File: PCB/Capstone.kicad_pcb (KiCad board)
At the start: 2 copper layers, 241 parts, among them J1 S2B-PH-SM4-TB, J10 DNP, J11 DNP, J12 PH1-08-UA, J13 DNP, J14 DNP, J15 DNP, J2 TRANSDUCER, J3 DNP, J4 PH1-08-UA, J5 DNP, J6 DNP, J7 DNP, J8 DNP, J9 DNP, Q1 SSM6K361NU, SW1 SW_Push, SW2 SW_Push, SW3 SW_Push, U1 TPS63031, U10 AP2204K-ADJ, U11 LM3478, U12 10CL010, U13 ECS-5032MV, U14 TSX9291, U15 LTC6090-5, U16 AD5450, U17 ADA4522-1, U18 MAX5394L, U19 MAX5394L, U2 TCR2EF25, U20 MAX11116, U21 TLV3544, U22 MCP6L1, U3 TPS62262, U4 BMD-360, U5 MIC841N, U6 ENS210, U7 W25Q80DV, U8 LIS2DE12, U9 LMR62421

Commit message: Begin layout around FPGA and microcontroller, rearrange some connections to FPGA and microcontroller, change groupings of optional debug pins
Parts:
- removed the C57 at (126.5, 83.0)
- removed the J12 at (82.3, 100.6)
- removed J15: DNP, Pin_Headers:Pin_Header_Straight_1x03_Pitch2.54mm
- added C51: 2.2nF, Capacitors_SMD:C_0603_HandSoldering, F.Cu at (131.2, 150.9)
- added C58: 22nF, Capacitors_SMD:C_0603_HandSoldering, F.Cu at (118.7, 152.3)
- added J14: DNP, Pin_Headers:Pin_Header_Straight_1x04_Pitch2.54mm, F.Cu at (186.1, 83.8)
- C49: value 2.2nF -> 100nF
- J10: footprint Pin_Headers:Pin_Header_Straight_1x03_Pitch2.54mm -> Pin_Headers:Pin_Header_Straight_1x05_Pitch2.54mm
- J11: footprint Pin_Headers:Pin_Header_Straight_1x03_Pitch2.54mm -> Pin_Headers:Pin_Header_Straight_2x05_Pitch2.54mm
- moved R13 111.3 mm to (85.1, 152.9), turned to 180 degrees
- moved SW2 107.7 mm to (85.1, 158.8), turned to 270 degrees
- moved R12 93.8 mm to (76.2, 152.9), turned to 180 degrees
- moved SW1 92.3 mm to (76.2, 158.8), turned to 270 degrees
- moved C49 79.9 mm to (133.3, 162.3), turned to 270 degrees
- moved J4 74.5 mm to (47.5, 128.5), turned to 0 degrees
- moved R38 73.5 mm to (136.4, 157.3), turned to 90 degrees
- moved J11 73.2 mm to (130.8, 160.0), turned to 270 degrees
- moved C59 70.7 mm to (131.2, 152.3), turned to 0 degrees
- moved C50 68.0 mm to (118.7, 150.9), turned to 180 degrees
- moved C47 67.4 mm to (135.0, 150.9), turned to 0 degrees
- moved C72 66.8 mm to (125.0, 152.0), turned to 270 degrees
- moved R39 66.1 mm to (126.7, 157.4), turned to 0 degrees
- moved C45 65.7 mm to (137.9, 148.3), turned to 0 degrees
- moved C60 65.3 mm to (139.6, 142.5), turned to 90 degrees
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- renumbered C99 to C100, C100 to C101, C101 to C102, C102 to C103, C103 to C104, C51 to C52, C52 to C53, C53 to C54, C54 to C55, C55 to C56, C56 to C57, C58 to C59, C59 to C60, C60 to C61, C61 to C62, C62 to C63, C63 to C64, C64 to C65, C65 to C66, C66 to C67, C67 to C68, C68 to C69, C69 to C70, C70 to C71, C71 to C72, C72 to C73, C73 to C74, C74 to C75, C75 to C76, C76 to C77, C77 to C78, C78 to C79, C79 to C80, C80 to C81, C81 to C82, C82 to C83, C83 to C84, C84 to C85, C85 to C86, C86 to C87, C87 to C88, C88 to C89, C89 to C90, C90 to C91, C91 to C92, C92 to C93, C93 to C94, C94 to C95, C95 to C96, C96 to C97, C97 to C98, C98 to C99, J13 to J12, J14 to J13
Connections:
- C47 pad 2: GND -> GNDA-FPGA
- C48 pad 2: GND -> GNDA-FPGA
- C49 pad 1: +1V2 -> +2V5
- C49 pad 2: GND -> GNDA-FPGA
- J10 pad 1: VGA-SCK -> VGA-~CS0
- J10 pad 3: VGA-~CS0 -> VGA-SCK
- J11 pad 1: TRANSMIT-ENABLE -> FPGA-TCK
- J11 pad 2: VGA-~CS1 -> GND
- J11 pad 3: VGA-D1 -> FPGA-TDO
- U12 pad 1: FPGA-LINK0 -> (no net)
- U12 pad 10: Net-(U12-Pad10) -> (no net)
- U12 pad 100: DAC-~CS -> (no net)
- U12 pad 101: DAC-SDI -> Net-(U12-Pad101)
- U12 pad 103: TRANSMIT-ENABLE -> Net-(U12-Pad103)
- U12 pad 106: DAC-SCK -> (no net)
- U12 pad 11: Net-(U12-Pad11) -> (no net)
- U12 pad 128: (no net) -> Net-(U12-Pad128)
- U12 pad 129: (no net) -> Net-(U12-Pad129)
- U12 pad 135: (no net) -> Net-(U12-Pad135)
- U12 pad 137: Net-(U12-Pad137) -> FPGA-LINK0
- U12 pad 138: Net-(U12-Pad138) -> FPGA-LINK1
- U12 pad 141: (no net) -> FPGA-LINK2
- U12 pad 142: (no net) -> FPGA-LINK3
- U12 pad 143: (no net) -> FPGA-LINK4
- U12 pad 144: (no net) -> FPGA-LINK5
- U12 pad 2: FPGA-LINK1 -> (no net)
- U12 pad 28: FPGA-LINK3 -> (no net)
- U12 pad 3: FPGA-LINK2 -> (no net)
- U12 pad 32: FPGA-LINK4 -> (no net)
- U12 pad 33: FPGA-LINK5 -> (no net)
- U12 pad 34: Net-(U12-Pad34) -> (no net)
- U12 pad 38: (no net) -> ADC-~CS
- U12 pad 39: (no net) -> ADC-SDO
- U12 pad 42: (no net) -> ADC-SCK
- U12 pad 43: (no net) -> Net-(U12-Pad43)
- U12 pad 44: (no net) -> Net-(U12-Pad44)
- U12 pad 49: (no net) -> Net-(U12-Pad49)
- U12 pad 50: (no net) -> Net-(U12-Pad50)
- U12 pad 51: (no net) -> VGA-D1
- U12 pad 52: (no net) -> VGA-~CS1
- U12 pad 53: (no net) -> VGA-SCK
- U12 pad 54: (no net) -> VGA-D0
- U12 pad 55: (no net) -> VGA-~CS0
- U12 pad 58: (no net) -> Net-(U12-Pad58)
- U12 pad 59: (no net) -> Net-(U12-Pad59)
- U12 pad 60: (no net) -> Net-(U12-Pad60)
- U12 pad 66: (no net) -> Net-(U12-Pad66)
- U12 pad 67: (no net) -> Net-(U12-Pad67)
- U12 pad 68: (no net) -> Net-(U12-Pad68)
- U12 pad 69: (no net) -> TRANSMIT-ENABLE
- U12 pad 70: (no net) -> DAC-SCK
- U12 pad 71: (no net) -> DAC-SDI
- U12 pad 72: (no net) -> DAC-~CS
- U12 pad 73: ADC-~CS -> (no net)
- U12 pad 74: ADC-SCK -> (no net)
- U12 pad 75: ADC-SDO -> (no net)
- U12 pad 76: Net-(U12-Pad76) -> (no net)
- U12 pad 77: Net-(U12-Pad77) -> (no net)
- U12 pad 83: VGA-~CS0 -> (no net)
- U12 pad 84: VGA-D0 -> (no net)
- U12 pad 85: VGA-SCK -> (no net)
- U12 pad 86: VGA-D1 -> Net-(U12-Pad86)
- U12 pad 87: VGA-~CS1 -> Net-(U12-Pad87)
- U4 pad 10: HV-ENABLE -> FPGA-CRC_ERROR
- U4 pad 11: /Microcontroller/HV-OK -> FPGA-INIT_DONE
- U4 pad 12: Net-(U4-Pad12) -> FPGA-CONF_DONE
- U4 pad 19: MICRO-TX -> MICRO-SCL
- U4 pad 20: MICRO-RX -> MICRO-SDA
- U4 pad 37: MICRO-SCL -> MICRO-TX
- U4 pad 38: MICRO-SDA -> MICRO-RX
- U4 pad 40: /Microcontroller/SW1 -> HV-ENABLE
- U4 pad 41: /Microcontroller/SW2 -> /Microcontroller/HV-OK
- U4 pad 42: FPGA-CONF_DONE -> Net-(U4-Pad42)
- U4 pad 6: FPGA-INIT_DONE -> /Microcontroller/SW1
- U4 pad 7: FPGA-nCONFIG -> /Microcontroller/SW2
- U4 pad 8: FPGA-nSTATUS -> FPGA-nCONFIG
- U4 pad 9: FPGA-CRC_ERROR -> FPGA-nSTATUS
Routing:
- net +3V3-LN: track 53.3 -> 0.00 mm
- net +1V2: track 0.00 -> 38.1 mm, vias 0 -> 8
- net +3V3: track 18.0 -> 55.4 mm
- net +50V: track 34.0 -> 0.00 mm
- net /Receive/MIDRAIL: track 24.6 -> 0.00 mm
- net /Transmit/MIDRAIL: track 21.4 -> 0.00 mm
- net FPGA-TCK: track 0.00 -> 18.5 mm
- net FPGA-TDI: track 0.00 -> 12.3 mm
- net FPGA-TDO: track 0.00 -> 11.7 mm
- net FPGA-TMS: track 0.00 -> 11.0 mm
- net Net-(R13-Pad1): track 0.00 -> 10.8 mm
- net Net-(R12-Pad1): track 0.00 -> 10.8 mm
- net Net-(C86-Pad2): track 10.6 -> 0.00 mm
- net /Microcontroller/SW2: track 0.00 -> 10.4 mm
- net TRANSMIT-ENABLE: track 10.4 -> 0.00 mm
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- added copper zone on In2.Cu, net +1V2
- added copper zone on In1.Cu, net GND
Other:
- copper layers 2 -> 4
- net class Default: clearance 0.2 -> 0.15; trace_width 0.25 -> 0.15
- net class Power added: clearance 0.2, trace_width 0.2, via_dia 0.8, via_drill 0.4
- rule trace_clearance: 0.2 -> 0.15
- rule trace_min: 0.2 -> 0.15
- rule via_min_size: 0.4 -> 0.6

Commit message: Remove unnecessary series resistors, rearrange connections on FPGA and microcontroller, rearrange debug pins, layout most of FPGA and microcontroller sections
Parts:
- removed the J12 at (81.8, 77.7)
- removed the R12 at (76.2, 152.9)
- removed the R13 at (85.1, 152.9)
- removed the R15 at (30.7, 64.5)
- removed the R32 at (88.6, 80.8)
- J5: footprint Pin_Headers:Pin_Header_Straight_1x08_Pitch2.54mm -> Pin_Headers:Pin_Header_Straight_1x15_Pitch2.54mm
- moved C22 90.7 mm to (101.6, 127.0)
- moved C25 86.3 mm to (97.8, 158.0), turned to 0 degrees
- moved D1 85.0 mm to (99.3, 127.0), turned to 270 degrees
- moved U6 83.5 mm to (97.8, 160.0)
- moved R5 82.6 mm to (98.4, 129.4), turned to 180 degrees
- moved R8 79.8 mm to (95.9, 127.8), turned to 180 degrees
- moved C26 79.7 mm to (97.8, 151.1), turned to 0 degrees
- moved R17 78.6 mm to (109.6, 161.9), turned to 180 degrees
- moved R11 78.0 mm to (95.9, 126.2), turned to 180 degrees
- moved SW3 77.0 mm to (94.2, 119.4), turned to 90 degrees
- moved U8 76.4 mm to (97.8, 153.7), turned to 90 degrees
- moved R7 75.7 mm to (93.2, 113.5), turned to 180 degrees
- moved R10 74.1 mm to (93.1, 127.9)
- moved U7 73.0 mm to (114.3, 158.8), turned to 90 degrees
- moved R31 71.5 mm to (101.2, 157.2), turned to 270 degrees
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- renumbered J13 to J12, J14 to J13, R14 to R12, R16 to R13, R17 to R14, R18 to R15, R19 to R16, R20 to R17, R21 to R18, R22 to R19, R23 to R20, R24 to R21, R25 to R22, R26 to R23, R27 to R24, R28 to R25, R29 to R26, R30 to R27, R31 to R28, R33 to R29, R34 to R30, R35 to R31, R36 to R32, R37 to R33, R38 to R34, R39 to R35, R40 to R36, R41 to R37, R42 to R38, R43 to R39, R44 to R40, R45 to R41, R46 to R42, R47 to R43, R48 to R44, R49 to R45, R50 to R46, R51 to R47, R52 to R48, R53 to R49, R54 to R50, R55 to R51, R56 to R52, R57 to R53, R58 to R54, R59 to R55, R60 to R56, R61 to R57, R62 to R58, R63 to R59, R64 to R60, R65 to R61, R66 to R62, R67 to R63, R68 to R64
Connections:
- J5 pad 1: FPGA-DOUT -> FPGA-CONF_DONE
- J5 pad 2: FPGA-DCLK -> FPGA-INIT_DONE
- J5 pad 3: FPGA-DIN -> FPGA-CRC_ERROR
- J5 pad 4: FPGA-CONF_DONE -> FPGA-LINK0
- J5 pad 5: FPGA-CRC_ERROR -> FPGA-LINK1
- J5 pad 6: FPGA-nSTATUS -> FPGA-LINK2
- J5 pad 7: FPGA-nCONFIG -> FPGA-LINK3
- J5 pad 8: FPGA-INIT_DONE -> FPGA-LINK4
- J6 pad 1: MICRO-SDA -> MICRO-SCL
- J6 pad 2: MICRO-SCL -> MICRO-SDA
- SW1 pad 1: Net-(R12-Pad1) -> /Microcontroller/SW1
- SW2 pad 1: Net-(R13-Pad1) -> /Microcontroller/SW2
- SW3 pad 1: Net-(R15-Pad1) -> MICRO-nRESET
- U12 pad 1: (no net) -> Net-(U12-Pad1)
- U12 pad 10: (no net) -> FPGA-CS
- U12 pad 11: (no net) -> FPGA-DOUT
- U12 pad 2: (no net) -> Net-(U12-Pad2)
- U12 pad 3: (no net) -> Net-(U12-Pad3)
- U12 pad 6: FPGA-CS -> Net-(U12-Pad6)
- U12 pad 8: FPGA-DOUT -> Net-(U12-Pad8)
- U4 pad 10: FPGA-CRC_ERROR -> FPGA-CONF_DONE
- U4 pad 12: FPGA-CONF_DONE -> FPGA-CRC_ERROR
- U4 pad 13: /Microcontroller/ACC-INT1 -> MICRO-SCL
- U4 pad 15: Net-(C23-Pad1) -> MICRO-SDA
- U4 pad 19: MICRO-SCL -> /Microcontroller/ACC-INT1
- U4 pad 20: MICRO-SDA -> Net-(C23-Pad1)
- U4 pad 21: FPGA-LINK0 -> FPGA-DIN
- U4 pad 22: FPGA-LINK1 -> FPGA-DCLK
- U4 pad 23: FPGA-LINK2 -> FPGA-DOUT
- U4 pad 24: FPGA-LINK3 -> FPGA-CS
- U4 pad 25: FPGA-LINK4 -> FPGA-LINK5
- U4 pad 26: FPGA-LINK5 -> FPGA-LINK4
- U4 pad 27: FPGA-DOUT -> FPGA-LINK3
- U4 pad 28: FPGA-DCLK -> FPGA-LINK2
- U4 pad 31: FPGA-DIN -> FPGA-LINK1
- U4 pad 32: FPGA-CS -> FPGA-LINK0
- U4 pad 34: /Microcontroller/LED-R -> /Microcontroller/LED-B
- U4 pad 36: /Microcontroller/LED-B -> /Microcontroller/LED-R
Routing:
- net FPGA-DIN: track 0.00 -> 62.1 mm
- net FPGA-nCONFIG: track 0.00 -> 58.8 mm, vias 0 -> 2
- net FPGA-CS: track 0.00 -> 58.8 mm, vias 0 -> 1
- net FPGA-DCLK: track 0.00 -> 53.8 mm
- net GND: track 90.3 -> 139.3 mm, vias 14 -> 50
- net +3V3: track 55.4 -> 103.4 mm, vias 0 -> 10
- net FPGA-DOUT: track 0.00 -> 47.6 mm
- net FPGA-CONF_DONE: track 0.00 -> 46.5 mm, vias 0 -> 1
- net FPGA-CRC_ERROR: track 0.00 -> 43.7 mm, vias 0 -> 1
- net FPGA-INIT_DONE: track 0.00 -> 43.0 mm, vias 0 -> 1
- net FPGA-nSTATUS: track 0.00 -> 40.1 mm, vias 0 -> 1
- net MICRO-SCL: track 0.00 -> 25.8 mm
- net MICRO-TX: track 0.00 -> 25.3 mm
- net MICRO-SDA: track 0.00 -> 25.0 mm
- net MICRO-RX: track 0.00 -> 24.7 mm
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- added copper zone on In2.Cu, net +3V3

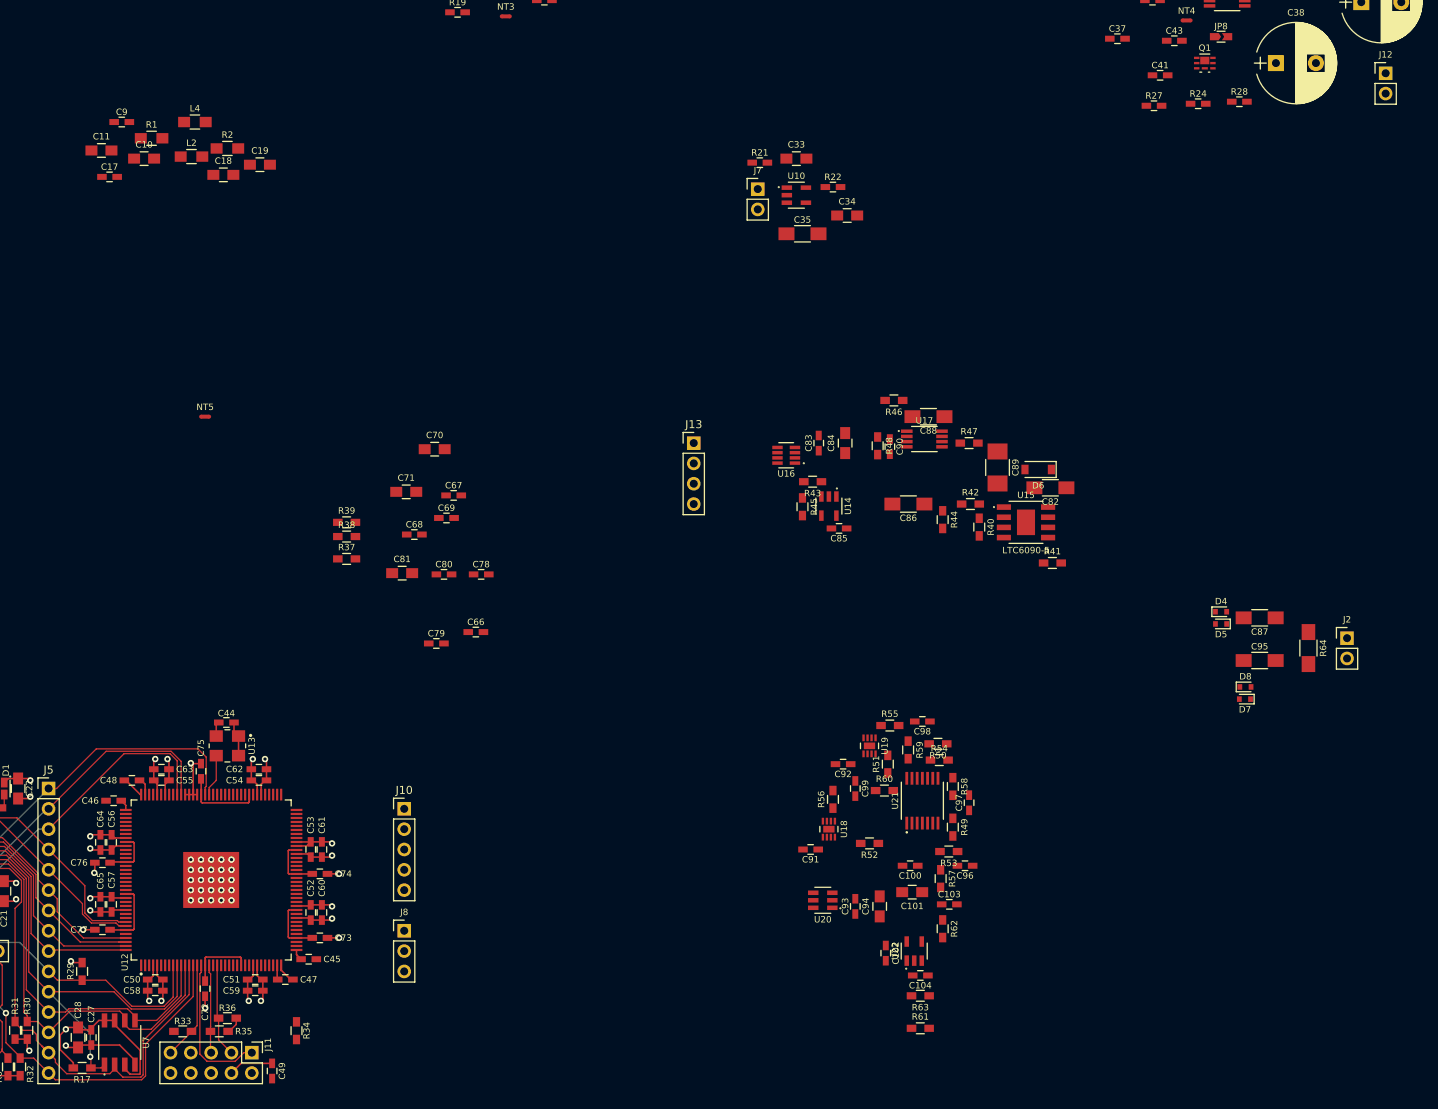
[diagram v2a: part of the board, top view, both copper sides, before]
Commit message: Rearrange FPGA connections, combine VGA and ADC debug headers, layout most of VGA and ADC circuits
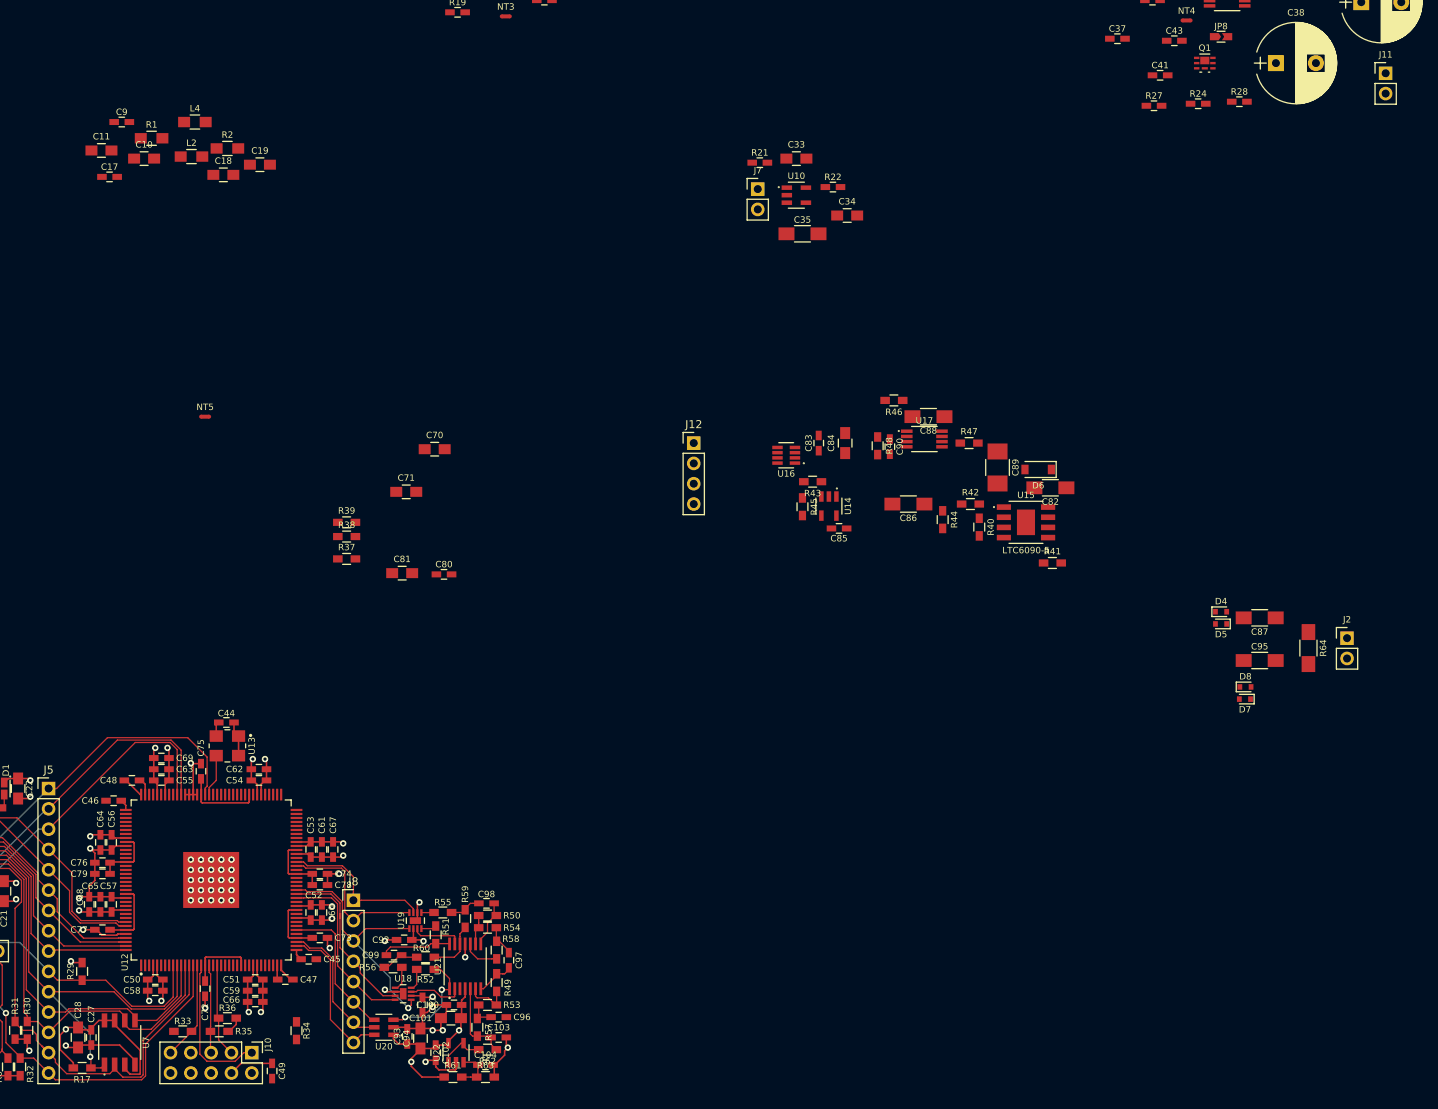
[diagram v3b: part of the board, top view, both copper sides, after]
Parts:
- removed the J10 at (149.9, 129.5)
- J8: value DNP -> PH1-08-UA; footprint Pin_Headers:Pin_Header_Straight_1x03_Pitch2.54mm -> Pin_Headers:Pin_Header_Straight_1x08_Pitch2.54mm
- moved C68 61.6 mm to (110.5, 141.5), turned to 90 degrees
- moved C99 61.3 mm to (148.6, 147.8), turned to 0 degrees
- moved C96 61.3 mm to (161.7, 155.6)
- moved R60 61.0 mm to (152.5, 148.1)
- moved U19 60.8 mm to (151.3, 143.5)
- moved R57 60.8 mm to (159.0, 156.8)
- moved C97 60.8 mm to (162.9, 148.5)
- moved U21 60.8 mm to (157.5, 149.2)
- moved R53 60.8 mm to (160.3, 154.1)
- moved R58 60.6 mm to (161.4, 147.2)
- moved R55 60.6 mm to (154.7, 142.5)
- moved R51 60.4 mm to (153.8, 145.3)
- moved R50 60.3 mm to (160.3, 142.9)
- moved R49 60.2 mm to (161.4, 151.3)
- moved R54 60.2 mm to (160.3, 144.4)
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- renumbered J11 to J10, J12 to J11, J13 to J12
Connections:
- J8 pad 1: ADC-SCK -> VGA-~CS0
- J8 pad 2: ADC-SDO -> VGA-D0
- J8 pad 3: ADC-~CS -> VGA-SCK
- U12 pad 50: Net-(U12-Pad50) -> VGA-D1
- U12 pad 51: VGA-D1 -> VGA-~CS1
- U12 pad 52: VGA-~CS1 -> VGA-SCK
- U12 pad 53: VGA-SCK -> Net-(U12-Pad53)
- U12 pad 54: VGA-D0 -> Net-(U12-Pad54)
- U12 pad 55: VGA-~CS0 -> Net-(U12-Pad55)
- U12 pad 58: Net-(U12-Pad58) -> VGA-D0
- U12 pad 59: Net-(U12-Pad59) -> VGA-~CS0
- U18 pad 9: (no net) -> GND
- U19 pad 9: (no net) -> GND
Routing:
- net GND: track 139.3 -> 191.0 mm, vias 50 -> 58
- net VGA-SCK: track 0.00 -> 34.0 mm, vias 0 -> 1
- net +3V3-LN: track 0.00 -> 23.2 mm, vias 0 -> 2
- net VGA-D1: track 0.00 -> 22.1 mm
- net VGA-~CS1: track 0.00 -> 21.8 mm
- net /Receive/MIDRAIL: track 0.00 -> 21.6 mm
- net VGA-D0: track 0.00 -> 20.3 mm
- net ADC-~CS: track 0.00 -> 19.5 mm
- net VGA-~CS0: track 0.00 -> 19.2 mm
- net ADC-SCK: track 0.00 -> 18.0 mm
- net ADC-SDO: track 0.00 -> 17.3 mm
- net Net-(R52-Pad1): track 0.00 -> 13.5 mm, vias 0 -> 2
- net Net-(C99-Pad1): track 0.00 -> 8.81 mm
- net +3V3: track 103.4 -> 112.0 mm, vias 10 -> 12
- net Net-(U18-Pad7): track 0.00 -> 6.84 mm
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
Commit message: Add additional mounting holes, optimize receive power supply connections for layout, simplify FPGA analog ground, layout 3v3 and 1v2 supplies
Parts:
- removed NT5: Net-Tie_2, Parts:NetTie-2
- added H3: MountingHole_Pad, Mounting_Holes:MountingHole_4mm_Pad_Via, F.Cu at (168.9, 100.3)
- added H4: MountingHole_Pad, Mounting_Holes:MountingHole_4mm_Pad_Via, F.Cu at (168.9, 158.8)
- moved R14 115.6 mm to (161.5, 91.4)
- moved C24 115.6 mm to (162.1, 82.3)
- moved U5 115.6 mm to (162.1, 86.9)
- moved R13 113.3 mm to (166.1, 83.8)
- moved R12 113.3 mm to (165.6, 80.5)
- moved R15 113.3 mm to (166.9, 87.9)
- moved R16 113.3 mm to (166.9, 91.4)
- moved H1 109.8 mm to (109.2, 100.3)
- moved J1 102.6 mm to (100.3, 102.9), turned to 180 degrees
- moved C4 97.6 mm to (112.0, 115.4)
- moved C1 97.1 mm to (100.1, 115.3)
- moved L1 97.1 mm to (102.9, 111.8)
- moved U1 97.1 mm to (102.9, 115.3)
- moved JP2 97.0 mm to (106.4, 113.7)
- moved C2 96.7 mm to (105.7, 116.7)
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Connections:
- C47 pad 2: GNDA-FPGA -> GND
- C48 pad 2: GNDA-FPGA -> GND
- C49 pad 2: GNDA-FPGA -> GND
- C91 pad 1: +3V3 -> +3V3-LN
- C92 pad 1: +3V3 -> +3V3-LN
- U12 pad 108: GNDA-FPGA -> GND
- U12 pad 36: GNDA-FPGA -> GND
- U18 pad 6: +3V3 -> +3V3-LN
- U19 pad 6: +3V3 -> +3V3-LN
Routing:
- net GND: track 191.0 -> 339.1 mm, vias 58 -> 81
- net +2V5: track 11.7 -> 123.6 mm, vias 0 -> 8
- net +1V2-LN: track 2.79 -> 48.3 mm
- net +1V2: track 43.7 -> 88.9 mm, vias 8 -> 11
- net +3V3: track 112.0 -> 153.8 mm, vias 12 -> 19
- net Net-(C23-Pad1): track 0.00 -> 34.4 mm, vias 0 -> 2
- net +BATT: track 0.00 -> 26.5 mm, vias 0 -> 7
- net Net-(C29-Pad1): track 0.00 -> 8.83 mm
- net +3V3-LN: track 23.2 -> 29.0 mm, vias 2 -> 4
- net GNDA-FPGA: track 5.40 -> 0.00 mm
- net Net-(C12-Pad1): track 0.00 -> 4.82 mm
- net Net-(C32-Pad2): track 0.00 -> 4.70 mm
- net Net-(JP2-Pad1): track 0.00 -> 4.59 mm
- net Net-(JP4-Pad1): track 0.00 -> 4.41 mm
- net +12V: track 0.00 -> 4.32 mm
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- added copper zone on B.Cu, net +3V3
- added copper zone on In2.Cu, net +3V3-LN
- added copper zone on In2.Cu, net +BATT
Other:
- board outline added: 87.6 x 68.6 mm
- net class Power: clearance 0.2 -> 0.15
